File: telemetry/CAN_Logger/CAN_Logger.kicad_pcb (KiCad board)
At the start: 2 copper layers, 81 x 58.4 mm, 61 parts, among them J1 CONN_02X03, J2 SD_socket, J3 MM_F_RA_20, U1 MCP2561-E_SN, U101 TPS560430YF, U2 ATMEGA16M1, U3 LM3480, U4 TXB0104, Y1 Crystal_SMD

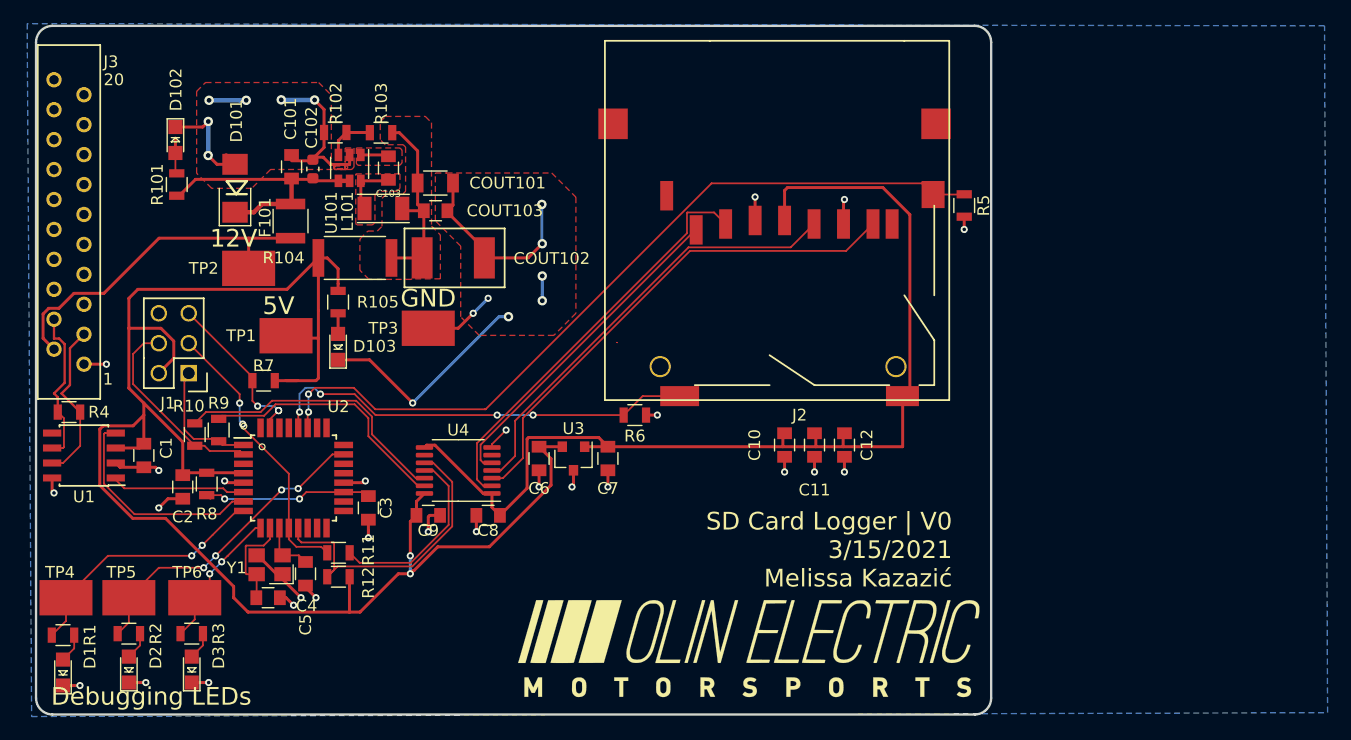
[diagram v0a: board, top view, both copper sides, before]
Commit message: Moved silks around to be more visible on PCB Layout
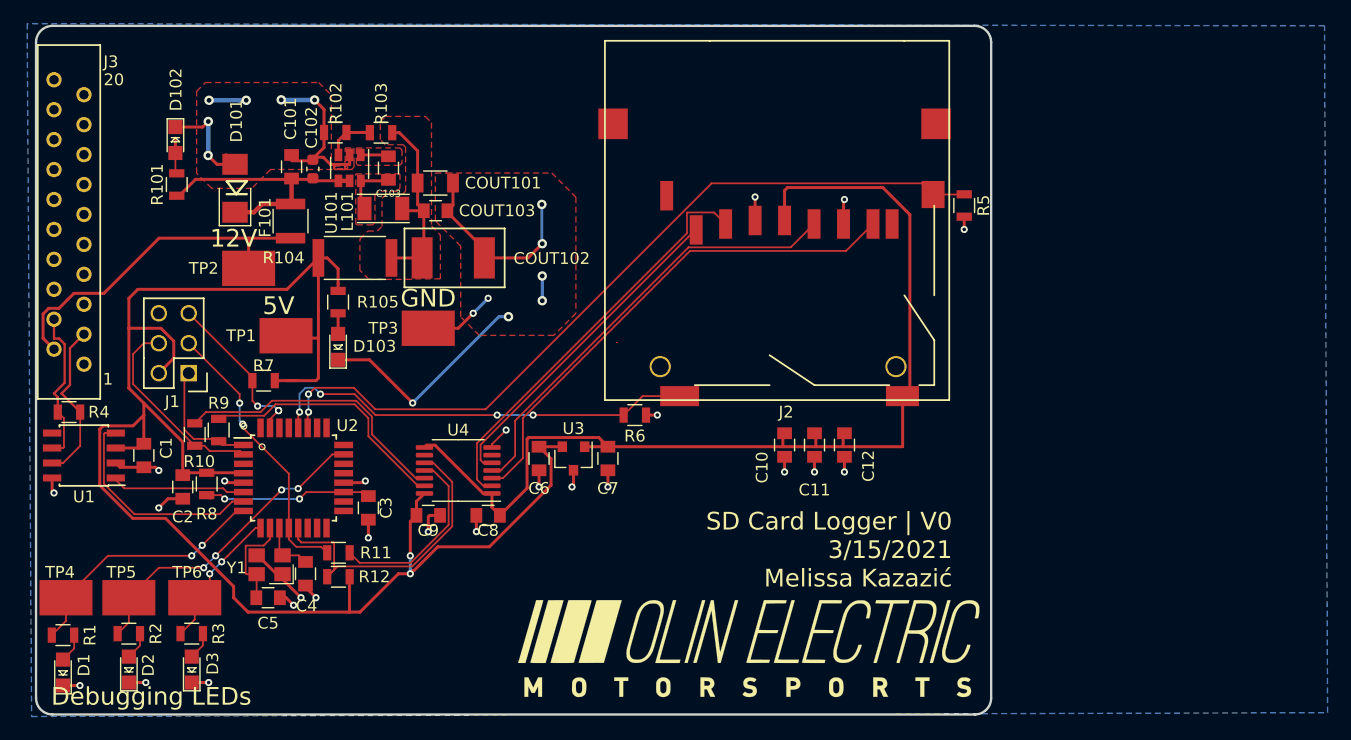
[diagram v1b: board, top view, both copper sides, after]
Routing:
- net GND: track 119.4 -> 117.5 mm, vias 40 -> 39

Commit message: Small tweaks for fabbing
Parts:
- moved R10 31.3 mm to (143.0, 111.2), turned to 270 degrees
- moved R9 31.2 mm to (145.0, 110.0), turned to 270 degrees
- moved J1 24.0 mm to (134.9, 109.9), turned to 270 degrees
- moved R11 16.5 mm to (139.4, 115.4)
- moved R8 15.8 mm to (128.4, 117.4), turned to 90 degrees
- moved C8 14.1 mm to (150.7, 118.4), turned to 270 degrees
- moved U4 11.8 mm to (145.9, 115.4)
- moved R7 9.78 mm to (126.9, 109.7), turned to 0 degrees
- moved C7 9.00 mm to (142.4, 121.0)
- moved U3 8.80 mm to (139.7, 120.9)
- moved C6 8.76 mm to (137.0, 121.0)
- moved R12 6.83 mm to (130.8, 123.4), turned to 90 degrees
- moved C9 4.50 mm to (127.5, 119.9), turned to 180 degrees
- moved TP2 3.22 mm to (113.2, 96.3)
- moved C2 1.93 mm to (112.3, 114.4), turned to 180 degrees
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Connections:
- U2 pad 13: /CS -> /CS_SD
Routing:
- net /MISO: track 10.5 -> 33.1 mm
- net +5V: track 148.8 -> 169.3 mm, vias 2 -> 4
- net /MOSI_SD: track 23.9 -> 6.67 mm
- net /MOSI: track 16.9 -> 33.7 mm
- net /MISO_SD: track 21.7 -> 7.18 mm
- net /SCK_SD: track 16.0 -> 2.67 mm
- net Net-(C3-Pad1): track 14.7 -> 4.22 mm, vias 2 -> 0
- net /MOSI_3V3: track 43.2 -> 34.9 mm
- net /SCK: track 23.9 -> 31.4 mm, vias 2 -> 0
- net /SD_PROTECT: track 67.8 -> 74.3 mm
- net /CAN_RX: track 18.6 -> 12.3 mm
- net /SCK_3V3: track 37.7 -> 32.2 mm
- net /CAN_TX: track 11.5 -> 16.8 mm
- net /MISO_3V3: track 35.2 -> 29.9 mm
- net +3V3: track 89.1 -> 93.7 mm, vias 0 -> 2
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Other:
- board text added: "DNP"
